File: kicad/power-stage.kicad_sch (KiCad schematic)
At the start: 13 parts, among them Q5 KND3508A, U8 PN7006A

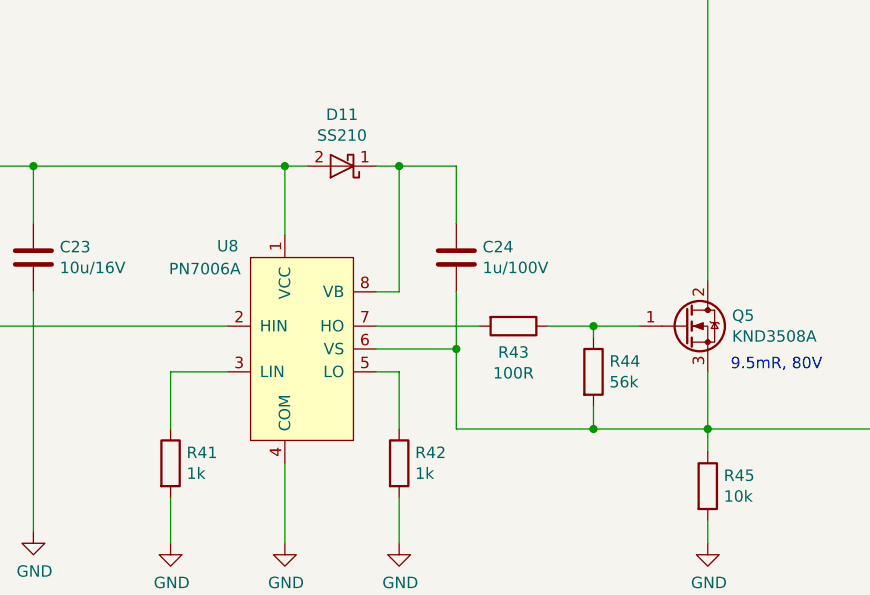
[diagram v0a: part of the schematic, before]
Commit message: BOM auf Lieferbarkeit aktualisiert, TODO: DRC bereinigen
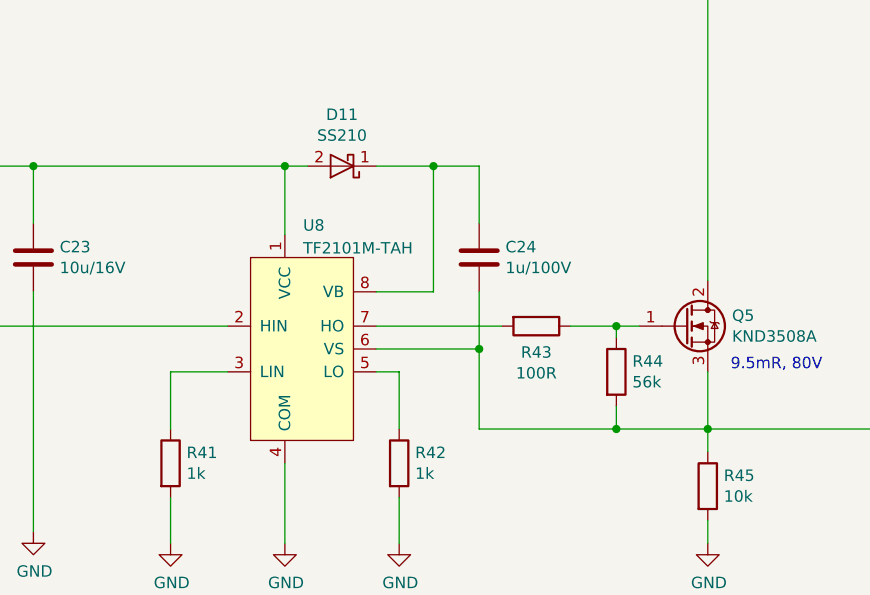
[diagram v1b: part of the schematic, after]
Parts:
- U8: value PN7006A -> TF2101M-TAH; DistOrderNr C414194 -> C2683752; PriceEUR 0.2188 -> 0.5072
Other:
- moved on the sheet: C24, R43, R44
